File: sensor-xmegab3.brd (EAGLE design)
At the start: 55.6 x 39.5 mm, 59 parts, among them IC3 ATmega169PA, K1 SP6029TOP, M1 NRF24L01P-M, M2 DHT22, Q1 IRLML2502, Q2 IRLML2502, Q3 IRLML6402, U1 MCP1640C, U2 MCP604-I/ST

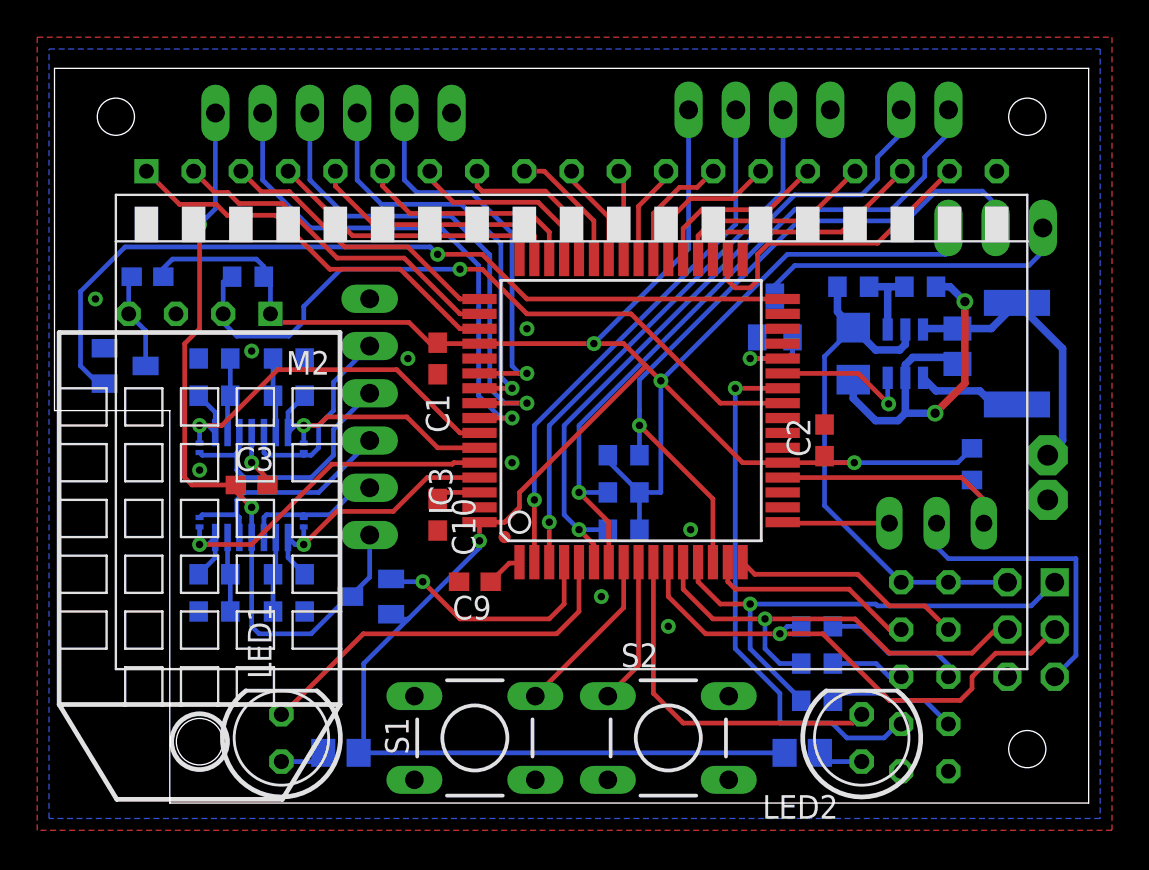
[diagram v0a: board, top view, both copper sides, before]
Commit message: hanged to xmega, better performance at lower price
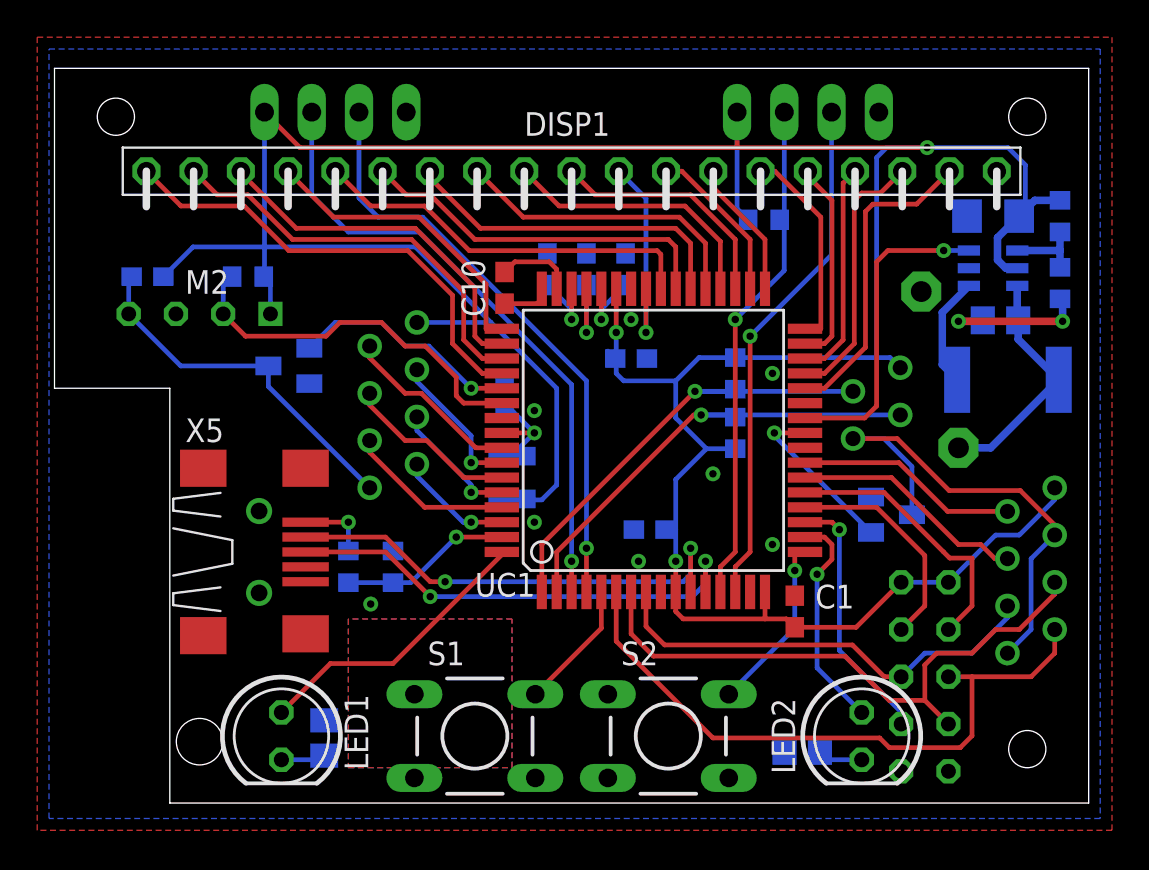
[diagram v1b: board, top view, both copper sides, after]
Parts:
- removed IC3: ATmega169PA, avr-7:TQFP64
- removed ISP: ML6, avr-7:AVR-ISP-6
- removed JP1: I2C, pinhead-mod:1X02
- removed JP2: 1-Wire, pinhead-mod:1X03
- removed JP3: serial, pinhead-mod:1X04
- removed JP4: ADC1, pinhead-mod:1X06
- removed JP5: ADC2, pinhead-mod:1X06
- removed JP6: (no value), jumper:JP2
- removed Q3: IRLML6402, mosfet:MICRO3
- removed R12, R7: 4k7, rcl:R0603
- removed R13, R14, R15, R16, R17, R18, R19, R20: (no value), rcl:R0603
- removed R21, R22, R23, R24: 0, rcl:R0201
- removed U2: MCP604-I/ST, microchip:SOP65P640X120-14N
- added C11, C12, C7: 100n, rcl:C0603
- added L2: 10u, inductor-neosid:SM-NE29
- added UC1: XMEGA-B3, avr-7:TQFP64
- added X1: serial, pinhead-mod:1X04
- added X2: SPI/1W, con-amp-micromatch:MICROMATCH-8
- added X3: I2C, con-amp-micromatch:MICROMATCH-4
- added X4: ADC, con-amp-micromatch:MICROMATCH-8
- added X5: (no value), con-usb:USB-MB-S
- added X6: PDI, pinhead-mod:1X04
- C9: value 1u -> 100n
- M2: value DHT22 -> DHT22-NP; device modules:DHT22 -> modules:DHT22-NOPRINT
- R5: value 4k7 -> 15k
- R6: value 4k7 -> 10k
- moved R5 25.4 mm to (16.0, 14.8), turned to 270 degrees
- moved R6 23.9 mm to (18.4, 14.8), turned to 270 degrees
- moved C1 23.5 mm to (40.0, 12.4), turned to 90 degrees
- moved C3 21.5 mm to (32.2, 16.8), flipped to the bottom
- moved R1 17.3 mm to (38.3, 33.5), turned to 180 degrees
- moved C9 17.2 mm to (26.7, 30.8), flipped to the bottom, turned to 270 degrees
- moved B- 13.1 mm to (46.8, 29.6)
- moved C10 12.7 mm to (24.4, 29.8)
- moved Q2 12.3 mm to (45.2, 17.6), turned to 90 degrees
- moved R9 11.7 mm to (54.3, 33.7), turned to 270 degrees
- moved C2 11.3 mm to (31.2, 26.0), flipped to the bottom, turned to 180 degrees
- moved C5 10.5 mm to (50.7, 33.7), turned to 0 degrees
- moved R8 10.3 mm to (36.8, 25.2), turned to 270 degrees
- moved Q1 8.80 mm to (12.8, 25.6), turned to 270 degrees
- moved R10 7.52 mm to (54.3, 30.1), turned to 90 degrees
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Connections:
- removed net !RESET: IC3.20, JP6.3, R1.2
- removed net 1WDATA: IC3.14, JP2.2, R12.2
- removed net 1WON: IC3.28, Q2.1
- removed net ADC6: IC3.55, JP5.4
- removed net ADC7: IC3.54, JP5.5
- removed net ADCON: IC3.4, Q3.1
- removed net AREF: C10.1, IC3.62
- removed net DHTON: IC3.32, Q1.1
- removed net LCDCAP: C9.1, IC3.1
- removed net N$13: LED1.A, R4.1
- removed net N$16: JP4.2, R21.1, U2.3
- removed net N$17: C3.1, JP4.1, JP5.1, Q3.3, U2.4
- removed net N$18: R16.2, R20.2, U2.13
- removed net N$19: R15.2, R19.2, U2.9
- removed net N$2: C8.1, M2.4, Q1.3
- removed net N$20: R14.2, R18.2, U2.6
- removed net N$21: R13.2, R17.2, U2.2
- removed net N$22: JP4.3, R22.1, U2.5
- removed net N$24: JP4.5, R23.1, U2.12
- removed net N$27: JP4.4, R24.1, U2.10
- removed net N$4: M1.MOSI, R7.1
- removed net N$5: M1.SCK, R5.1
- removed net SSEXT: IC3.17, JP6.1
- new net AVCC: C7.1, L2.2, UC1.56
- new net DHTADCON: Q1.1, UC1.53
- new net N$10: C12.2, UC1.44
- new net N$12: C8.1, M2.4, Q1.3, X4.8
- new net N$14: C9.2, UC1.46
- new net N$23: C10.1, UC1.47
- new net N$25: C10.2, UC1.48
- new net N$9: C11.2, UC1.45
- new net PDIC: R1.2, UC1.13, X6.2
- new net PDID: UC1.14, X6.3
- new net SPI1WON: Q2.1, UC1.25
- new net SS1WA: UC1.22, X2.4
- new net SS1WB: UC1.23, X2.2
- new net USBD_N: UC1.11, X5.D-
- new net USBD_P: UC1.12, X5.D+
- new net USBV: R5.2, R6.2, UC1.63
- net ADC0: now also UC1.57, X4.2; no longer IC3.61, R17.1, R21.2, U2.1
- net ADC1: now also UC1.58, X4.3; no longer IC3.60, R18.1, R22.2, U2.7
- net ADC2: now also UC1.59, X4.4; no longer IC3.59, R20.1, R23.2, U2.14
- net ADC3: now also UC1.60, X4.5; no longer IC3.58, R19.1, R24.2, U2.8
- net ADC4: now also UC1.61, X4.6; no longer IC3.57, JP5.2
- net ADC5: now also UC1.62, X4.7; no longer IC3.56, JP5.3
- net COM0: now also DISP1.4, UC1.49; no longer DISP1.1, IC3.51
- net COM1: now also DISP1.3, UC1.50; no longer DISP1.2, IC3.50
- net COM2: now also DISP1.2, UC1.51; no longer DISP1.3, IC3.49
- net COM3: now also DISP1.1, UC1.52; no longer DISP1.4, IC3.48
- net GND: now also C11.1, C12.1, C7.2, C9.1, R3.2, R4.2, R6.1, UC1.15, UC1.42, UC1.55, UC1.9, X1.4, X5.GND, X6.4; no longer C10.2, C9.2, IC3.22, IC3.53, IC3.63, ISP.6, JP3.4, JP4.6, JP5.6, R13.1, R14.1, R15.1, R16.1, U2.11
- net ICP: now also UC1.54; no longer IC3.25
- net LED1: now also LED1.A, UC1.64; no longer IC3.5, LED1.K
- net LED2: now also LED2.A, UC1.18; no longer IC3.10, LED2.K
- net MISO: now also M1.MISO, UC1.7, X2.5; no longer IC3.13, ISP.1, R6.2
- net MOSI: now also M1.MOSI, UC1.8, X2.6; no longer IC3.12, ISP.4, R7.2
- net N$1: now also LED1.K, R4.1; no longer LED2.A, R3.1
- net N$11: now also X2.3, X2.8, X3.4; no longer JP2.3
- net N$3: now also R5.1, X5.VBUS; no longer M1.MISO, R6.1
- net N$6: now also LED2.K, R3.1; no longer ISP.5, JP6.2
- net PWRON: now also UC1.26; no longer IC3.27
- net RFCE: now also UC1.21; no longer IC3.16
- net RFCSN: now also UC1.20; no longer IC3.15
- net RFIRQ: now also UC1.19; no longer IC3.26
- net RXD: now also UC1.3, X1.2; no longer IC3.2, JP3.2
- net SCK: now also M1.SCK, UC1.6, X2.7; no longer IC3.11, ISP.3, R5.2
- net SCL: now also R11.2, UC1.2, X3.3; no longer IC3.6, JP1.1, R8.2
- net SDA: now also R8.2, UC1.1, X3.2; no longer IC3.7, JP1.2, R11.2
- net SEG0: now also UC1.40; no longer IC3.47
- net SEG1: now also UC1.39; no longer IC3.46
- net SEG10: now also UC1.31; no longer IC3.37
- net SEG11: now also UC1.30; no longer IC3.36
- net SEG12: now also UC1.29; no longer IC3.35
- net SEG13: now also UC1.28; no longer IC3.34
- net SEG14: now also UC1.27; no longer IC3.33
- net SEG2: now also UC1.38; no longer IC3.45
- net SEG3: now also UC1.37; no longer IC3.44
- net SEG4: now also UC1.36; no longer IC3.43
- net SEG5: now also UC1.35; no longer IC3.42
- net SEG6: now also UC1.41; no longer IC3.41
- net SEG7: now also UC1.34; no longer IC3.40
- net SEG8: now also UC1.33; no longer IC3.39
- net SEG9: now also UC1.32; no longer IC3.38
- net SW1: now also UC1.5; no longer IC3.8
- net SW2: now also S2.2, UC1.17; no longer IC3.9, S2.1
- net TXD: now also UC1.4, X1.3; no longer IC3.3, JP3.3
- net VCC: now also C3.1, L2.1, UC1.10, UC1.16, UC1.43, X1.1, X2.1, X3.1, X4.1, X6.1; no longer IC3.21, IC3.52, IC3.64, ISP.2, JP2.1, JP3.1, Q3.2, R12.1, R3.2, R4.2
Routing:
- net DHTON: track 45.6 -> 0.00 mm, vias 1 -> 0
- net N$17: track 41.7 -> 0.00 mm, vias 2 -> 0
- net 1WDATA: track 38.0 -> 0.00 mm, vias 1 -> 0
- net PDIC: track 0.00 -> 28.1 mm, vias 0 -> 1
- net PDID: track 0.00 -> 27.9 mm, vias 0 -> 1
- net USBD_P: track 0.00 -> 25.6 mm, vias 0 -> 2
- net USBD_N: track 0.00 -> 25.6 mm, vias 0 -> 2
- net ADC6: track 22.5 -> 0.00 mm, vias 1 -> 0
- net ADC7: track 21.2 -> 0.00 mm, vias 1 -> 0
- net ADC5: track 27.0 -> 6.23 mm
- net N$12: track 0.00 -> 19.5 mm
- net ADC4: track 28.2 -> 8.96 mm, vias 1 -> 0
- net ICP: track 38.1 -> 20.4 mm, vias 1 -> 0
- net GND: track 23.5 -> 8.20 mm, vias 12 -> 10
- net ADC3: track 22.2 -> 6.92 mm
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- added copper zone on layer 1, net N$2
- added copper zone on layer 16, net N$5
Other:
- outline, holes or cut-outs redrawn

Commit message: some rerouting
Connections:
- removed net SEG14: UC1.27
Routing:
- net SDA: track 24.9 -> 23.1 mm
- net SCL: track 25.6 -> 24.1 mm
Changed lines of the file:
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@@
 <wire x1="19.6" y1="32" x2="11.49" y2="32" width="0.254" layer="16"/>
 <wire x1="19.6" y1="32" x2="23.66" y2="27.94" width="0.254" layer="16"/>
-<wire x1="23.66" y1="27.94" x2="27.2" y2="24.4" width="0.254" layer="16"/>
-<wire x1="27.2" y1="24.4" x2="27.2" y2="19.2" width="0.254" layer="16"/>
-<wire x1="27.2" y1="19.2" x2="26.4" y2="18.4" width="0.254" layer="16"/>
+<wire x1="23.66" y1="27.94" x2="27.4" y2="24.2" width="0.254" layer="16"/>
+<wire x1="27.4" y1="24.2" x2="27.4" y2="19.4" width="0.254" layer="16"/>
+<wire x1="27.4" y1="19.4" x2="26.4" y2="18.4" width="0.254" layer="16"/>
 <wire x1="26.4" y1="18.4" x2="24.85" y2="18.4" width="0.254" layer="16"/>
 <wire x1="24.85" y1="18.4" x2="24.8" y2="18.45" width="0.254" layer="16"/>
@@
 <wire x1="30.4" y1="26.05" x2="30.4" y2="25.2" width="0.254" layer="16"/>
 <wire x1="30.4" y1="25.2" x2="30.8" y2="24.8" width="0.254" layer="16"/>
-<wire x1="30.8" y1="24.8" x2="33.6" y2="24.8" width="0.254" layer="16"/>
-<wire x1="33.6" y1="24.8" x2="34.85" y2="26.05" width="0.254" layer="16"/>
-<wire x1="34.85" y1="26.05" x2="36.8" y2="26.05" width="0.254" layer="16"/>
-<wire x1="36.8" y1="21.15" x2="35.25" y2="21.15" width="0.254" layer="16"/>
-<wire x1="35.25" y1="21.15" x2="33.6" y2="22.8" width="0.254" layer="16"/>
-<wire x1="33.6" y1="22.8" x2="33.6" y2="24.8" width="0.254" layer="16"/>
+<wire x1="30.8" y1="24.8" x2="34.7" y2="24.8" width="0.254" layer="16"/>
+<wire x1="34.7" y1="24.8" x2="35.95" y2="26.05" width="0.254" layer="16"/>
+<wire x1="35.95" y1="26.05" x2="36.8" y2="26.05" width="0.254" layer="16"/>
+<wire x1="36.8" y1="21.15" x2="34.7" y2="21.15" width="0.254" layer="16"/>
+<wire x1="34.7" y1="21.15" x2="34.7" y2="24.8" width="0.254" layer="16"/>
 <wire x1="45.67" y1="25.505" x2="45.125" y2="26.05" width="0.254" layer="16"/>
 <wire x1="45.125" y1="26.05" x2="44.4" y2="26.05" width="0.254" layer="16"/>
 <wire x1="44.4" y1="26.05" x2="36.8" y2="26.05" width="0.254" layer="16"/>
-<wire x1="35.25" y1="21.15" x2="33.6" y2="19.5" width="0.254" layer="16"/>
-<wire x1="33.6" y1="19.5" x2="33.6" y2="16.8" width="0.254" layer="16"/>
+<wire x1="33.6" y1="20.05" x2="33.6" y2="16.8" width="0.254" layer="16"/>
 <wire x1="33.6" y1="16.8" x2="33.6" y2="15.1" width="0.254" layer="16"/>
 <wire x1="33.6" y1="15.1" x2="33.6" y2="13.45" width="0.254" layer="1"/>
@@
 <wire x1="36.897" y1="39.245" x2="36.897" y2="37.405" width="0.254" layer="1"/>
 <wire x1="36.897" y1="37.405" x2="36.83" y2="37.338" width="0.254" layer="1"/>
+<wire x1="34.7" y1="21.15" x2="33.6" y2="20.05" width="0.254" layer="16"/>
 </signal>
 <signal name="RFCE">
@@
 <signal name="SDA">
 <contactref element="UC1" pad="1"/>
-<wire x1="26.4" y1="13.45" x2="26.4" y2="16" width="0.254" layer="1"/>
+<wire x1="26.4" y1="13.45" x2="26.4" y2="16.2" width="0.254" layer="1"/>
 <contactref element="R8" pad="2"/>
 <contactref element="X3" pad="2"/>
-<wire x1="43.13" y1="24.235" x2="34.635" y2="24.235" width="0.254" layer="16"/>
-<wire x1="34.635" y1="24.235" x2="26.4" y2="16" width="0.254" layer="1"/>
-<via x="34.635" y="24.235" extent="1-16" drill="0.4"/>
-<wire x1="34.635" y1="24.235" x2="36.685" y2="24.235" width="0.254" layer="16"/>
+<wire x1="43.13" y1="24.235" x2="36.685" y2="24.235" width="0.254" layer="16"/>
 <wire x1="36.685" y1="24.235" x2="36.8" y2="24.35" width="0.254" layer="16"/>
+<wire x1="26.4" y1="16.2" x2="34.6" y2="24.4" width="0.254" layer="1"/>
+<wire x1="36.685" y1="24.235" x2="36.52" y2="24.4" width="0.254" layer="16"/>
+<wire x1="36.52" y1="24.4" x2="35.5" y2="24.4" width="0.254" layer="16"/>
+<via x="35.5" y="24.4" extent="1-16" drill="0.4"/>
+<wire x1="35.5" y1="24.4" x2="34.6" y2="24.4" width="0.254" layer="1"/>
 </signal>
 <signal name="TXD">
@@
 <wire x1="17.6" y1="33.6" x2="20" y2="33.6" width="0.254" layer="16"/>
 <wire x1="20" y1="33.6" x2="28.8" y2="24.8" width="0.254" layer="16"/>
-<wire x1="28.8" y1="24.8" x2="28.8" y2="15.8" width="0.254" layer="16"/>
-<via x="28.8" y="15.8" extent="1-16" drill="0.4"/>
-<wire x1="28.8" y1="15.8" x2="28.8" y2="13.45" width="0.254" layer="1"/>
+<wire x1="28.8" y1="24.8" x2="28.8" y2="16" width="0.254" layer="16"/>
+<via x="28.8" y="16" extent="1-16" drill="0.4"/>
+<wire x1="28.8" y1="16" x2="28.8" y2="13.45" width="0.254" layer="1"/>
 </signal>
 <signal name="RXD">
@@
 <wire x1="16" y1="32.8" x2="19.8" y2="32.8" width="0.254" layer="16"/>
 <wire x1="19.8" y1="32.8" x2="28" y2="24.6" width="0.254" layer="16"/>
-<wire x1="28" y1="24.6" x2="28" y2="15.1" width="0.254" layer="16"/>
-<via x="28" y="15.1" extent="1-16" drill="0.4"/>
-<wire x1="28" y1="15.1" x2="28" y2="13.45" width="0.254" layer="1"/>
+<wire x1="28" y1="24.6" x2="28" y2="15.3" width="0.254" layer="16"/>
+<via x="28" y="15.3" extent="1-16" drill="0.4"/>
+<wire x1="28" y1="15.3" x2="28" y2="13.45" width="0.254" layer="1"/>
 </signal>
 <signal name="N$7">
@@
 <signal name="SCL">
 <contactref element="UC1" pad="2"/>
-<wire x1="27.2" y1="15.6" x2="27.2" y2="13.45" width="0.254" layer="1"/>
+<wire x1="27.2" y1="16" x2="27.2" y2="13.45" width="0.254" layer="1"/>
 <contactref element="R11" pad="2"/>
 <contactref element="X3" pad="3"/>
-<wire x1="34.965" y1="22.965" x2="45.67" y2="22.965" width="0.254" layer="16"/>
-<via x="34.965" y="22.965" extent="1-16" drill="0.4"/>
-<wire x1="27.2" y1="15.6" x2="34.565" y2="22.965" width="0.254" layer="1"/>
-<wire x1="34.565" y1="22.965" x2="34.965" y2="22.965" width="0.254" layer="1"/>
-<wire x1="34.965" y1="22.965" x2="36.685" y2="22.965" width="0.254" layer="16"/>
+<wire x1="36.685" y1="22.965" x2="45.67" y2="22.965" width="0.254" layer="16"/>
+<wire x1="27.2" y1="16" x2="34" y2="22.8" width="0.254" layer="1"/>
 <wire x1="36.685" y1="22.965" x2="36.8" y2="22.85" width="0.254" layer="16"/>
+<wire x1="36.685" y1="22.965" x2="36.52" y2="22.8" width="0.254" layer="16"/>
+<wire x1="36.52" y1="22.8" x2="35.5" y2="22.8" width="0.254" layer="16"/>
+<via x="35.5" y="22.8" extent="1-16" drill="0.4"/>
+<wire x1="35.5" y1="22.8" x2="34" y2="22.8" width="0.254" layer="1"/>
 </signal>
 <signal name="LED1">
@@
 <wire x1="45.72" y1="6.35" x2="45.72" y2="6.985" width="0.254" layer="16"/>
 <wire x1="45.72" y1="6.985" x2="42.4" y2="10.305" width="0.254" layer="16"/>
-</signal>
-<signal name="SEG14">
-<contactref element="UC1" pad="27"/>
 </signal>
 <signal name="AVCC">
@@
 <contactref element="UC1" pad="14"/>
 <contactref element="X6" pad="3"/>
-<wire x1="41.977" y1="31.577" x2="37.6" y2="27.2" width="0.254" layer="16"/>
-<via x="37.6" y="27.2" extent="1-16" drill="0.4"/>
+<wire x1="41.977" y1="31.577" x2="40" y2="29.6" width="0.254" layer="16"/>
+<wire x1="40" y1="29.6" x2="37.6" y2="27.2" width="0.254" layer="1"/>
 <wire x1="37.6" y1="27.2" x2="37.6" y2="15.6" width="0.254" layer="1"/>
 <wire x1="37.6" y1="15.6" x2="36.8" y2="14.8" width="0.254" layer="1"/>
 <wire x1="36.8" y1="14.8" x2="36.8" y2="13.45" width="0.254" layer="1"/>
 <wire x1="41.977" y1="39.245" x2="41.977" y2="31.577" width="0.254" layer="16"/>
+<via x="40" y="29.6" extent="1-16" drill="0.4"/>
 </signal>
 <signal name="DHTADCON">

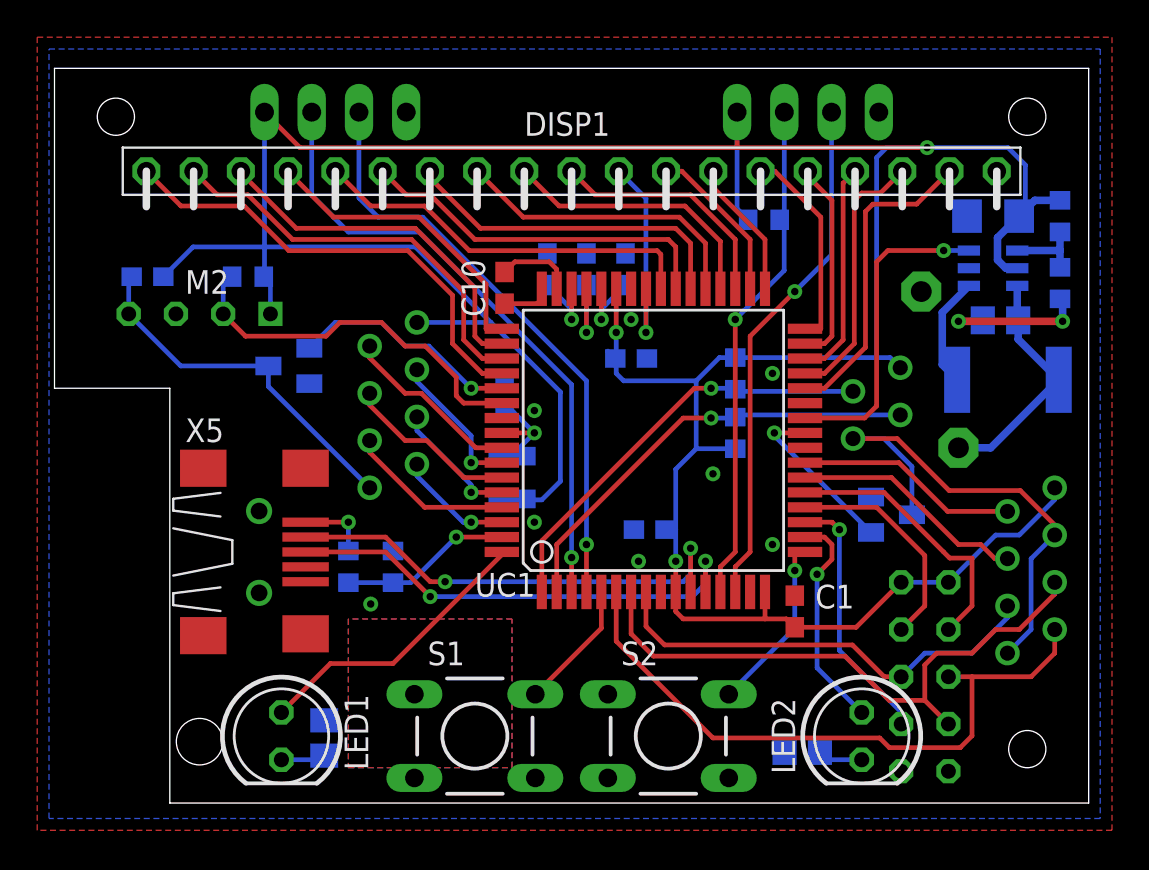
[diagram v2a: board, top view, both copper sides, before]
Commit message: sensor-xmega3 top+bottom silk screen arranged
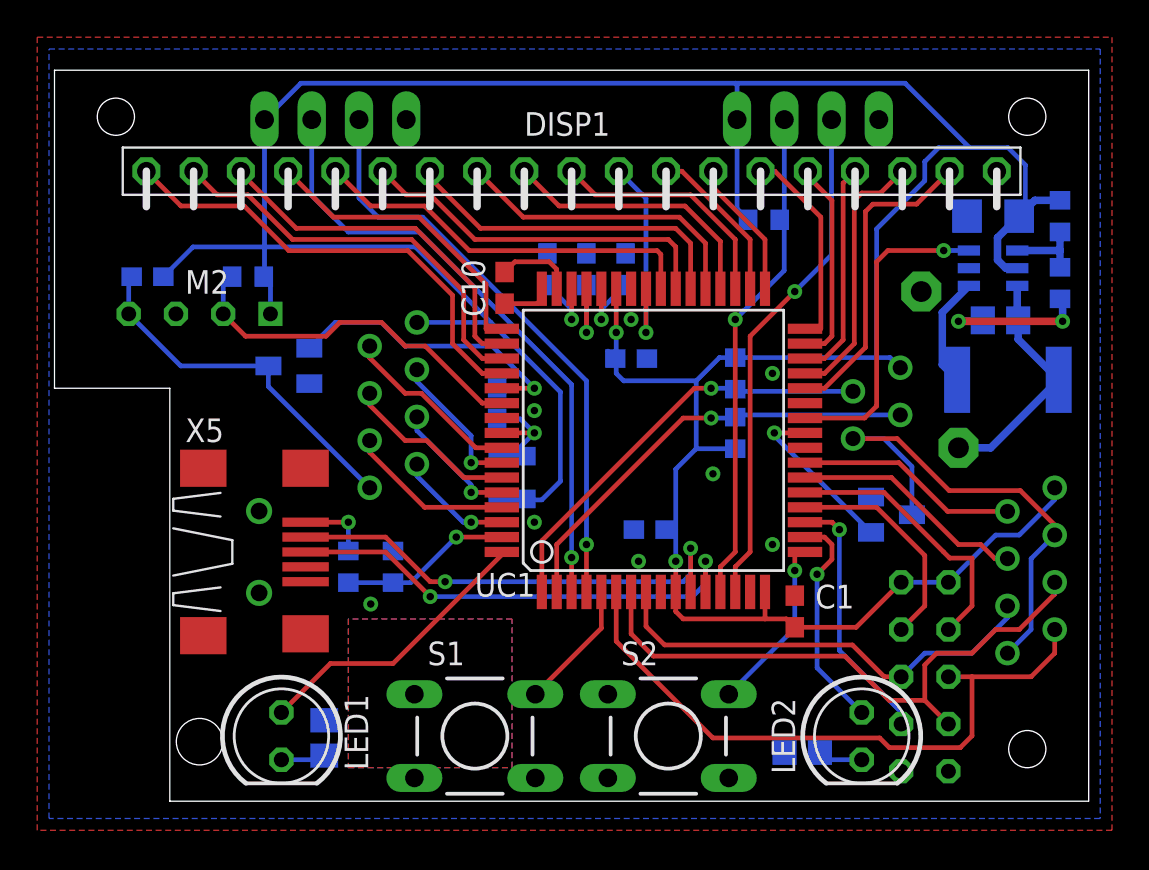
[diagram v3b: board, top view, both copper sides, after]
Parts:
- moved C7 0.57 mm to (24.0, 23.6)
- moved X1 0.40 mm to (15.3, 38.8)
- moved X6 0.40 mm to (40.7, 38.8)
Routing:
- net DHTADCON: track 12.4 -> 15.9 mm
- net VCC: track 184.5 -> 185.8 mm, vias 3 -> 2
- net ICP: track 20.4 -> 19.8 mm
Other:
- board size 55.6 x 39.5 mm -> 55.6 x 39.3 mm
